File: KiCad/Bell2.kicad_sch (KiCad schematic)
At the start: 34 parts, among them J1 USB-C, J2 POWER, J3 Conn_01x10, U1 ESP32-PICO-MINI-02, U2 FT231XQ, U3 ISL89410, U4 ISL89410, U5 LMR16006+FB, U6 AA, U7 QR

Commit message: Started Keypad2 - may scrap it though.
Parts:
- R10: value 324R -> 220R
- R8: value 732R -> 680R
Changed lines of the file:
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@@
     (in_bom yes) (on_board yes)
     (property "Reference" "R10" (id 0) (at 191.77 102.235 90))
-    (property "Value" "324R" (id 1) (at 191.77 104.775 90))
+    (property "Value" "220R" (id 1) (at 191.77 104.775 90))
     (property "Footprint" "RevK:R_0603" (id 2) (at 191.77 102.997 90)
       (effects (font (size 1.27 1.27)) hide)
@@
     (in_bom yes) (on_board yes)
     (property "Reference" "R8" (id 0) (at 191.77 92.075 90))
-    (property "Value" "732R" (id 1) (at 191.77 94.615 90))
+    (property "Value" "680R" (id 1) (at 191.77 94.615 90))
     (property "Footprint" "RevK:R_0603" (id 2) (at 191.77 92.837 90)
       (effects (font (size 1.27 1.27)) hide)
@@
     )
     (path "/00000000-0000-0000-0000-000060ce4fe8"
-      (reference "R8") (unit 1) (value "732R") (footprint "RevK:R_0603")
+      (reference "R8") (unit 1) (value "680R") (footprint "RevK:R_0603")
     )
     (path "/00000000-0000-0000-0000-000060ce4750"
@@
     )
     (path "/00000000-0000-0000-0000-000060819c12"
-      (reference "R10") (unit 1) (value "324R") (footprint "RevK:R_0603")
+      (reference "R10") (unit 1) (value "220R") (footprint "RevK:R_0603")
     )
     (path "/c1897ab9-a710-4f2b-b18b-f2f520d0a247"

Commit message: Bell2 - tracks and DRC
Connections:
- net B: now also U1.34 (IO22); no longer U1.17 (IO27)
- net G: now also U1.35 (IO21); no longer U1.13 (IO33)
- net IN1: now also U1.27 (IO7); no longer U1.33 (IO19)
- net OUT1: now also U1.18 (IO14); no longer U1.35 (IO21)
- net OUT2: now also U1.20 (IO13); no longer U1.34 (IO22)
- net OUT3: now also U1.21 (IO15); no longer U1.15 (IO25)
- net OUT4: now also U1.28 (IO8); no longer U1.16 (IO26)
- net R: now also U1.33 (IO19); no longer U1.12 (IO32)
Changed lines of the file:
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@@
     )
   )
-  (global_label "R" (shape input) (at 66.04 76.2 0) (fields_autoplaced)
-    (effects (font (size 1.27 1.27)) (justify left))
-    (property "Intersheet References" "${INTERSHEET_REFS}" (id 0) (at -2.54 -2.54 0)
+  (global_label "R" (shape input) (at 66.04 58.42 0) (fields_autoplaced)
+    (effects (font (size 1.27 1.27)) (justify left))
+    (property "Intersheet References" "${INTERSHEET_REFS}" (id 0) (at -2.54 -20.32 0)
       (effects (font (size 1.27 1.27)) hide)
     )
@@
     )
   )
-  (global_label "IN1" (shape input) (at 66.04 58.42 0) (fields_autoplaced)
-    (effects (font (size 1.27 1.27)) (justify left))
-    (property "Intersheet References" "${INTERSHEET_REFS}" (id 0) (at -2.54 5.08 0)
+  (global_label "IN1" (shape input) (at 35.56 68.58 180) (fields_autoplaced)
+    (effects (font (size 1.27 1.27)) (justify right))
+    (property "Intersheet References" "${INTERSHEET_REFS}" (id 0) (at 104.14 121.92 0)
       (effects (font (size 1.27 1.27)) hide)
     )
@@
     )
   )
-  (global_label "B" (shape input) (at 66.04 73.66 0) (fields_autoplaced)
-    (effects (font (size 1.27 1.27)) (justify left))
-    (property "Intersheet References" "${INTERSHEET_REFS}" (id 0) (at -2.54 -2.54 0)
+  (global_label "B" (shape input) (at 66.04 66.04 0) (fields_autoplaced)
+    (effects (font (size 1.27 1.27)) (justify left))
+    (property "Intersheet References" "${INTERSHEET_REFS}" (id 0) (at -2.54 -10.16 0)
       (effects (font (size 1.27 1.27)) hide)
     )
@@
     )
   )
-  (global_label "OUT3" (shape input) (at 66.04 68.58 0) (fields_autoplaced)
-    (effects (font (size 1.27 1.27)) (justify left))
-    (property "Intersheet References" "${INTERSHEET_REFS}" (id 0) (at -2.54 -2.54 0)
+  (global_label "OUT3" (shape input) (at 35.56 81.28 180) (fields_autoplaced)
+    (effects (font (size 1.27 1.27)) (justify right))
+    (property "Intersheet References" "${INTERSHEET_REFS}" (id 0) (at 104.14 152.4 0)
       (effects (font (size 1.27 1.27)) hide)
     )
@@
     )
   )
-  (global_label "OUT2" (shape input) (at 66.04 66.04 0) (fields_autoplaced)
-    (effects (font (size 1.27 1.27)) (justify left))
-    (property "Intersheet References" "${INTERSHEET_REFS}" (id 0) (at -2.54 -2.54 0)
+  (global_label "OUT2" (shape input) (at 35.56 76.2 180) (fields_autoplaced)
+    (effects (font (size 1.27 1.27)) (justify right))
+    (property "Intersheet References" "${INTERSHEET_REFS}" (id 0) (at 104.14 144.78 0)
       (effects (font (size 1.27 1.27)) hide)
     )
@@
     )
   )
-  (global_label "G" (shape input) (at 66.04 78.74 0) (fields_autoplaced)
-    (effects (font (size 1.27 1.27)) (justify left))
-    (property "Intersheet References" "${INTERSHEET_REFS}" (id 0) (at -2.54 -2.54 0)
-      (effects (font (size 1.27 1.27)) hide)
-    )
-  )
-  (global_label "OUT1" (shape input) (at 66.04 63.5 0) (fields_autoplaced)
-    (effects (font (size 1.27 1.27)) (justify left))
-    (property "Intersheet References" "${INTERSHEET_REFS}" (id 0) (at -2.54 -2.54 0)
+  (global_label "G" (shape input) (at 66.04 63.5 0) (fields_autoplaced)
+    (effects (font (size 1.27 1.27)) (justify left))
+    (property "Intersheet References" "${INTERSHEET_REFS}" (id 0) (at -2.54 -17.78 0)
+      (effects (font (size 1.27 1.27)) hide)
+    )
+  )
+  (global_label "OUT1" (shape input) (at 35.56 78.74 180) (fields_autoplaced)
+    (effects (font (size 1.27 1.27)) (justify right))
+    (property "Intersheet References" "${INTERSHEET_REFS}" (id 0) (at 104.14 144.78 0)
       (effects (font (size 1.27 1.27)) hide)
     )
@@
     )
   )
-  (global_label "OUT4" (shape input) (at 66.04 71.12 0) (fields_autoplaced)
-    (effects (font (size 1.27 1.27)) (justify left))
-    (property "Intersheet References" "${INTERSHEET_REFS}" (id 0) (at -2.54 -2.54 0)
-      (effects (font (size 1.27 1.27)) hide)
-    )
+  (global_label "OUT4" (shape input) (at 35.56 71.12 180) (fields_autoplaced)
+    (effects (font (size 1.27 1.27)) (justify right))
+    (property "Intersheet References" "${INTERSHEET_REFS}" (id 0) (at 104.14 144.78 0)
+      (effects (font (size 1.27 1.27)) hide)
+    )

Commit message: Checking
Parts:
- AJK1, U6: Note (none) -> Non part, PCB printed
- U2: footprint RevK:QFN-20-1EP_4x4mm_P0.5mm_EP2.5x2.5mm -> Package_DFN_QFN:QFN-20-1EP_4x4mm_P0.5mm_EP2.5x2.5mm
- U7: Note (none) -> Non part, PCB printed; now left out of the parts list
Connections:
- no-connect marks 5 -> 20
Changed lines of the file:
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@@
   (no_connect (at 83.82 173.99))
   (no_connect (at 126.365 52.705))
+  (no_connect (at 66.04 78.74))
+  (no_connect (at 66.04 71.12))
+  (no_connect (at 66.04 73.66))
+  (no_connect (at 66.04 76.2))
+  (no_connect (at 35.56 66.04))
+  (no_connect (at 35.56 63.5))
+  (no_connect (at 35.56 60.96))
+  (no_connect (at 35.56 73.66))
+  (no_connect (at 35.56 53.34))
+  (no_connect (at 35.56 48.26))
+  (no_connect (at 35.56 45.72))
+  (no_connect (at 35.56 40.64))
+  (no_connect (at 35.56 43.18))
+  (no_connect (at 35.56 50.8))
+  (no_connect (at 66.04 68.58))
   (no_connect (at 126.365 50.165))
   (no_connect (at 83.82 171.45))
@@
       (effects (font (size 1.27 1.27)) hide)
     )
+    (property "Note" "Non part, PCB printed" (id 4) (at 266.7 175.26 0)
+      (effects (font (size 1.27 1.27)) hide)
+    )
   )
   (symbol (lib_id "RevK:PowerIn") (at 201.93 24.13 0) (unit 1)
@@
     (property "Reference" "U2" (id 0) (at 54.61 183.515 0))
     (property "Value" "FT231XQ" (id 1) (at 62.23 169.545 0))
-    (property "Footprint" "RevK:QFN-20-1EP_4x4mm_P0.5mm_EP2.5x2.5mm" (id 2) (at 100.33 181.61 0)
+    (property "Footprint" "Package_DFN_QFN:QFN-20-1EP_4x4mm_P0.5mm_EP2.5x2.5mm" (id 2) (at 100.33 181.61 0)
       (effects (font (size 1.27 1.27)) hide)
     )
@@
       (effects (font (size 1.27 1.27)) hide)
     )
-    (property "Value" "AA" (id 1) (at 269.875 175.26 0)
+    (property "Value" "AA" (id 1) (at 269.24 175.26 0)
       (effects (font (size 1.27 1.27)) (justify left))
     )
@@
     )
     (property "Datasheet" "" (id 3) (at 269.24 175.26 0)
+      (effects (font (size 1.27 1.27)) hide)
+    )
+    (property "Note" "Non part, PCB printed" (id 4) (at 269.24 175.26 0)
       (effects (font (size 1.27 1.27)) hide)
     )
@@
   )
   (symbol (lib_id "RevK:QR") (at 280.67 175.26 0) (unit 1)
-    (in_bom yes) (on_board yes)
+    (in_bom no) (on_board yes)
     (property "Reference" "U7" (id 0) (at 280.67 178.435 0)
       (effects (font (size 1.27 1.27)) hide)
@@
     )
     (property "Datasheet" "" (id 3) (at 280.035 175.895 0)
+      (effects (font (size 1.27 1.27)) hide)
+    )
+    (property "Note" "Non part, PCB printed" (id 4) (at 280.67 175.26 0)
       (effects (font (size 1.27 1.27)) hide)
     )
@@
     (pin "2")
   )
-  (symbol (lib_name "Hidden_2") (lib_id "RevK:Hidden") (at 256.54 29.845 0) (unit 1)
+  (symbol (lib_id "RevK:Hidden") (at 256.54 29.845 0) (unit 1)
     (in_bom yes) (on_board yes)
     (property "Reference" "C4" (id 0) (at 257.175 29.845 0)
@@
     (pin "~")
   )
-  (symbol (lib_name "Hidden_4") (lib_id "RevK:Hidden") (at 256.54 31.75 0) (unit 1)
+  (symbol (lib_id "RevK:Hidden") (at 256.54 31.75 0) (unit 1)
     (in_bom yes) (on_board yes)
     (property "Reference" "C5" (id 0) (at 257.175 31.75 0)
@@
     (pin "~")
   )
-  (symbol (lib_name "Hidden_3") (lib_id "RevK:Hidden") (at 256.54 33.655 0) (unit 1)
+  (symbol (lib_id "RevK:Hidden") (at 256.54 33.655 0) (unit 1)
     (in_bom yes) (on_board yes)
     (property "Reference" "C6" (id 0) (at 257.175 33.655 0)
@@
     (pin "~")
   )
-  (symbol (lib_name "Hidden_1") (lib_id "RevK:Hidden") (at 256.54 35.56 0) (unit 1)
+  (symbol (lib_id "RevK:Hidden") (at 256.54 35.56 0) (unit 1)
     (in_bom yes) (on_board yes)
     (property "Reference" "L1" (id 0) (at 257.175 35.56 0)
@@
     )
     (path "/00000000-0000-0000-0000-00006084108b"
-      (reference "U2") (unit 1) (value "FT231XQ") (footprint "RevK:QFN-20-1EP_4x4mm_P0.5mm_EP2.5x2.5mm")
+      (reference "U2") (unit 1) (value "FT231XQ") (footprint "Package_DFN_QFN:QFN-20-1EP_4x4mm_P0.5mm_EP2.5x2.5mm")
     )
     (path "/00000000-0000-0000-0000-000060ce050a"

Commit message: Tidy
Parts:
- removed U2: FT231XQ, Package_DFN_QFN:QFN-20-1EP_4x4mm_P0.5mm_EP2.5x2.5mm, symbol Interface_USB:FT231XQ
- added U2: FT231XQ, RevK:QFN-20-1EP_4x4mm_P0.5mm_EP2.5x2.5mm, symbol RevK:FT231XQ
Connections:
- net +3V3: now also U2.10 (3V3OUT), U2.11 (~{RESET}), U2.12 (VCC), U2.20 (VCCIO)
- net BOOT: now also U2.18 (~{DTR})
- net D+: now also U2.8 (USBDP)
- net D-: now also U2.9 (USBDM)
- net EN: now also U2.19 (~{RTS})
- net GND: now also U2.13 (GND), U2.2 (~{RI}), U2.21 (GND), U2.3 (GND), U2.4 (~{DSR}), U2.5 (~{DCD}), U2.6 (~{CTS})
- net I: now also U2.17 (TXD)
- net O: now also U2.1 (RXD)
- net at R2.2, R3.1: now also U2.16 (CBUS3)
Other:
- moved on the sheet: C1, R2, R3

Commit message: Tidy
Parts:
- J1: symbol Connector:USB_C_Receptacle_USB2.0 -> RevK:USB-C
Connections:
- net GND: no longer U1.54 (GND), U1.55 (GND), U1.56 (GND), U1.57 (GND), U1.58 (GND), U1.59 (GND), U1.60 (GND), U1.61 (GND)
- no-connect marks 20 -> 18
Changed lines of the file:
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@@
   (no_connect (at 81.28 165.1))
   (no_connect (at 81.28 170.18))
-  (no_connect (at 126.365 52.705))
   (no_connect (at 66.04 78.74))
   (no_connect (at 66.04 71.12))
@@
   (no_connect (at 35.56 50.8))
   (no_connect (at 66.04 68.58))
-  (no_connect (at 126.365 50.165))
   (no_connect (at 81.28 167.64))
   (wire (pts (xy 126.365 29.845) (xy 128.905 29.845))
@@
     )
   )
-  (symbol (lib_id "Connector:USB_C_Receptacle_USB2.0") (at 111.125 37.465 0) (unit 1)
+  (symbol (lib_id "RevK:USB-C") (at 111.125 37.465 0) (unit 1)
     (in_bom yes) (on_board yes)
     (property "Reference" "J1" (id 0) (at 113.8428 15.4432 0))
@@
   (symbol (lib_id "RevK:PowerIn") (at 201.93 24.13 0) (unit 1)
     (in_bom yes) (on_board yes)
-    (property "Reference" "J2" (id 0) (at 203.962 24.3332 0)
-      (effects (font (size 1.27 1.27)) (justify left))
-    )
-    (property "Value" "POWER" (id 1) (at 203.962 26.6446 0)
+    (property "Reference" "J2" (id 0) (at 200.66 20.32 0)
+      (effects (font (size 1.27 1.27)) (justify left))
+    )
+    (property "Value" "POWER" (id 1) (at 200.66 30.48 0)
       (effects (font (size 1.27 1.27)) (justify left))
     )
@@
   (symbol (lib_id "Driver_FET:EL7202CN") (at 113.665 88.265 0) (unit 1)
     (in_bom yes) (on_board yes)
-    (property "Reference" "U3" (id 0) (at 113.665 73.5076 0))
-    (property "Value" "ISL89410" (id 1) (at 113.665 75.819 0))
+    (property "Reference" "U3" (id 0) (at 106.68 99.06 0))
+    (property "Value" "ISL89410" (id 1) (at 119.38 99.06 0))
     (property "Footprint" "Package_SO:SO-8_3.9x4.9mm_P1.27mm" (id 2) (at 113.665 95.885 0)
       (effects (font (size 1.27 1.27)) hide)
@@
   (symbol (lib_id "Driver_FET:EL7202CN") (at 154.305 88.265 0) (unit 1)
     (in_bom yes) (on_board yes)
-    (property "Reference" "U4" (id 0) (at 154.305 73.5076 0))
-    (property "Value" "ISL89410" (id 1) (at 154.305 75.819 0))
+    (property "Reference" "U4" (id 0) (at 147.32 99.06 0))
+    (property "Value" "ISL89410" (id 1) (at 160.02 99.06 0))
     (property "Footprint" "Package_SO:SO-8_3.9x4.9mm_P1.27mm" (id 2) (at 154.305 95.885 0)
       (effects (font (size 1.27 1.27)) hide)
@@
     (pin "52")
     (pin "53")
-    (pin "54")
-    (pin "55")
-    (pin "56")
-    (pin "57")
-    (pin "58")
-    (pin "59")
     (pin "6")
-    (pin "60")
-    (pin "61")
     (pin "7")
     (pin "8")

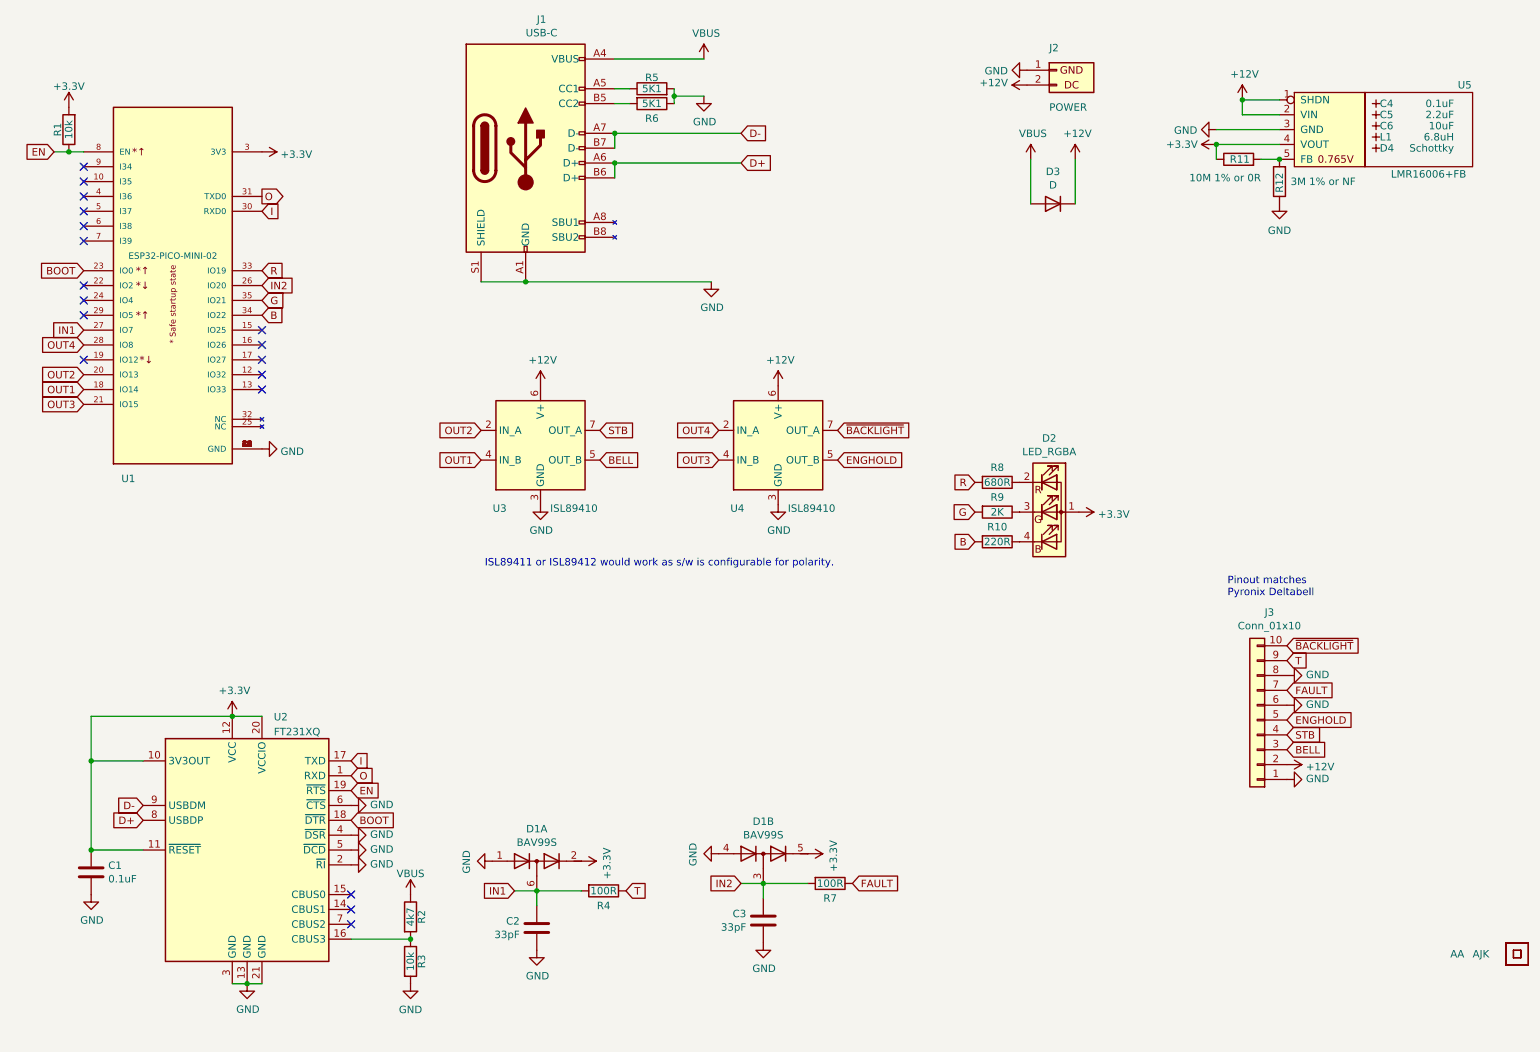
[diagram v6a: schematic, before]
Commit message: Bell box with GPS add on
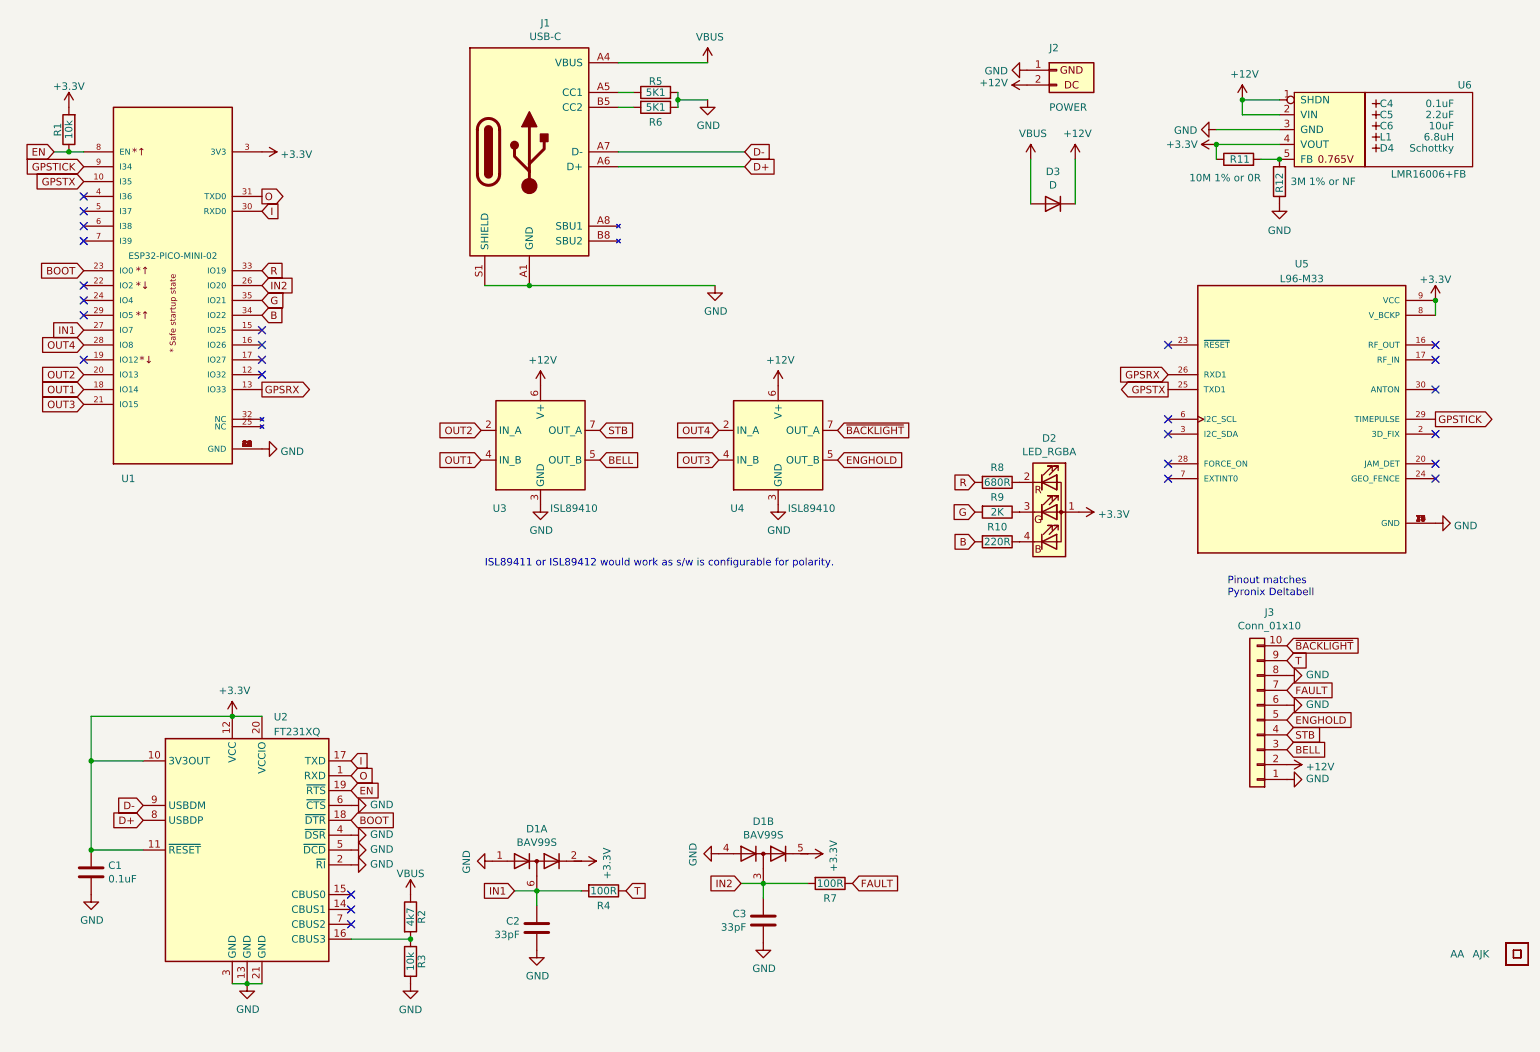
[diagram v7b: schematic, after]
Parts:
- added U5: L96-M33, RevK:L96-M33, symbol RevK:L96-M33
- renumbered U5 to U6, U6 to U7, U7 to U8
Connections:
- net +3V3: now also U5.8 (V_BCKP), U5.9 (VCC)
- net GND: now also U5.10 (GND), U5.11 (GND), U5.12 (GND), U5.13 (GND), U5.14 (GND), U5.15 (GND), U5.18 (GND), U5.19 (GND), U5.21 (GND), U5.22 (GND), U5.27 (GND), U5.31 (GND), U5.4 (GND), U5.5 (GND)
- net GPSTX: now reaches U1.10 (I35)
- net GPSTX: now also U5.25 (TXD1)
- net GPSRX: now reaches U1.13 (IO33)
- net GPSRX: now also U5.26 (RXD1)
- net GPSTICK: now reaches U1.9 (I34)
- net GPSTICK: now also U5.29 (TIMEPULSE)
- no-connect marks 18 -> 26
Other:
- moved on the sheet: R5, R6
